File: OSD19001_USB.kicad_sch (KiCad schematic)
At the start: 11 parts, among them J1 ${PARTNUMBER}, U1 ${PARTNUMBER}

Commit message: Fixed schematic symbol values: were set to Altium variables
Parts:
- C10, C5, C6, C7: value ${ALTIUM_VALUE} -> 0.22uF
- C8, C9: value ${ALTIUM_VALUE} -> 10uF
- D3: value ${PARTNUMBER} -> ECMF02-2AMX6
- J1: value ${PARTNUMBER} -> UJ2-MIBH2-4-SMT
- L1: value ${PARTNUMBER} -> MPZ1608S102ATA00
- R13: value ${ALTIUM_VALUE} -> 12K
- U1: value ${PARTNUMBER} -> OSD32MP157C-512M-BAA
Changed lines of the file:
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@@
       (effects (font (size 1.27 1.27)) (justify left bottom))
     )
-    (property "Value" "${ALTIUM_VALUE}" (id 1) (at 139.954 144.272 0)
+    (property "Value" "12K" (id 1) (at 139.954 144.272 0)
       (effects (font (size 1.27 1.27)) (justify left bottom))
     )
@@
       (effects (font (size 1.27 1.27)) (justify left bottom))
     )
-    (property "Value" "${ALTIUM_VALUE}" (id 1) (at 126.492 144.272 0)
+    (property "Value" "0.22uF" (id 1) (at 126.492 144.272 0)
       (effects (font (size 1.27 1.27)) (justify left bottom))
     )
@@
       (effects (font (size 1.27 1.27)) (justify left bottom))
     )
-    (property "Value" "${ALTIUM_VALUE}" (id 1) (at 231.648 116.332 0)
+    (property "Value" "0.22uF" (id 1) (at 231.648 116.332 0)
       (effects (font (size 1.27 1.27)) (justify left bottom))
     )
@@
       (effects (font (size 1.27 1.27)) (justify left bottom))
     )
-    (property "Value" "${ALTIUM_VALUE}" (id 1) (at 257.048 116.078 0)
+    (property "Value" "0.22uF" (id 1) (at 257.048 116.078 0)
       (effects (font (size 1.27 1.27)) (justify left bottom))
     )
@@
       (effects (font (size 1.27 1.27)) (justify left bottom))
     )
-    (property "Value" "${ALTIUM_VALUE}" (id 1) (at 269.748 116.078 0)
+    (property "Value" "0.22uF" (id 1) (at 269.748 116.078 0)
       (effects (font (size 1.27 1.27)) (justify left bottom))
     )
@@
       (effects (font (size 1.27 1.27)) (justify left bottom))
     )
-    (property "Value" "${ALTIUM_VALUE}" (id 1) (at 282.194 116.332 0)
+    (property "Value" "10uF" (id 1) (at 282.194 116.332 0)
       (effects (font (size 1.27 1.27)) (justify left bottom))
     )
@@
       (effects (font (size 1.27 1.27)) (justify left bottom))
     )
-    (property "Value" "${ALTIUM_VALUE}" (id 1) (at 294.894 116.332 0)
+    (property "Value" "10uF" (id 1) (at 294.894 116.332 0)
       (effects (font (size 1.27 1.27)) (justify left bottom))
     )
@@
       (effects (font (size 1.27 1.27)) (justify left bottom))
     )
-    (property "Value" "${PARTNUMBER}" (id 1) (at 233.172 104.14 0)
+    (property "Value" "MPZ1608S102ATA00" (id 1) (at 233.172 104.14 0)
       (effects (font (size 1.27 1.27)) (justify left bottom))
     )
@@
       (effects (font (size 1.27 1.27)) (justify left bottom))
     )
-    (property "Value" "${PARTNUMBER}" (id 1) (at 175.006 119.38 0)
+    (property "Value" "ECMF02-2AMX6" (id 1) (at 175.006 119.38 0)
       (effects (font (size 1.27 1.27)) (justify left bottom))
     )
@@
       (effects (font (size 1.27 1.27)) (justify left bottom))
     )
-    (property "Value" "${PARTNUMBER}" (id 1) (at 108.458 114.3 0)
+    (property "Value" "UJ2-MIBH2-4-SMT" (id 1) (at 108.458 114.3 0)
       (effects (font (size 1.27 1.27)) (justify left bottom))
     )
@@
       (effects (font (size 1.27 1.27)) (justify left bottom))
     )
-    (property "Value" "${PARTNUMBER}" (id 1) (at 192.786 185.42 0)
+    (property "Value" "OSD32MP157C-512M-BAA" (id 1) (at 192.786 185.42 0)
       (effects (font (size 1.27 1.27)) (justify right bottom))
     )

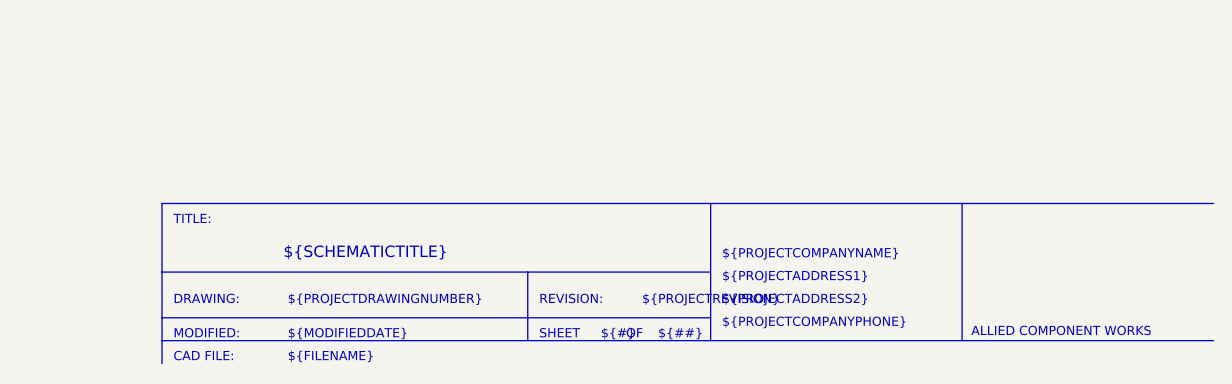
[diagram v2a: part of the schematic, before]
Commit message: Corrected title bar text to match online PDF schematic
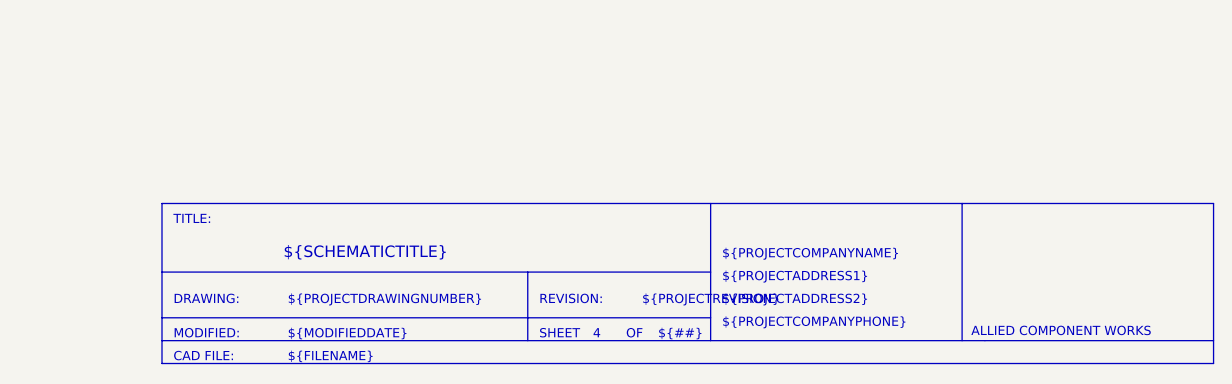
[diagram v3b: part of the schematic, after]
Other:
- note added: "4"
- note removed: "${#}"
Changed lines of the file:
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@@
+    (stroke (width 0) (type solid) (color 0 0 0 0))
+  )
+  (polyline (pts (xy 375.92 256.54) (xy 375.92 274.32))
+    (stroke (width 0) (type solid) (color 0 0 0 0))
+  )
+  (polyline (pts (xy 375.92 274.32) (xy 259.08 274.32))
     (stroke (width 0) (type solid) (color 0 0 0 0))
   )
@@
     (effects (font (size 1.016 1.016)) (justify left bottom))
   )
-  (text "${#}" (at 307.848 271.78 180)
-    (effects (font (size 1.016 1.016)) (justify left bottom))
+  (text "4" (at 307.848 271.78 180)
+    (effects (font (size 1.016 1.016)) (justify right bottom))
   )
   (text "OF" (at 310.642 271.78 180)
